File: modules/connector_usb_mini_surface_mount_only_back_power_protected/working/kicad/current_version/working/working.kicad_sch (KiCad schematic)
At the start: 2 parts, among them J3 scumnsmo

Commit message: a few module workings
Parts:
- removed D1: dssod123pmb2, oomlout_oomp_part_footprints:dssod123pmb2_electronic_diode_schottky_sod_123_package_marking_b2_mbr0520, symbol oomlout_oomp_part_symbols:dssod123pmb2_electronic_diode_schottky_sod_123_packag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
- removed J3: scumnsmo, oomlout_oomp_part_kicad_footprints:scumnsmo_electronic_socket_usb_mini_surface_mount_only, symbol oomlout_oomp_part_symbols:scumnsmo_electronic_socket_usb_mini_surface_mount_only
- added J1: scumnsmo, scumnsmo_electronic_socket_usb_mini_surface_mount_only, symbol oomlout_oomp_part_symbols:scumnsmo_electronic_socket_usb_mini_surface_mount_only
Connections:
- net +5V: now also J1.1 (VBUS)
- net GND: now also J1.5 (GND)
- net usb_id: now also J1.4 (ID)
- net usb_negative: now also J1.2 (D-)
- net usb_plus: now also J1.3 (D+)
- new net usb_shield: J1.6 (Shield)
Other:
- note added: "module connector usb_mini surface_mount_only"
- note removed: "module connector usb_mini surface_mount_only back_power_protected"
- note removed: "name"
- note removed: "usb_mini"
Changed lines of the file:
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@@
 (kicad_sch (version 20230121) (generator eeschema)
   (paper "A4")
-  (junction (at 146.05 114.3) (diameter 0) (color 0 0 0 0)
-  )
-  (wire (pts (xy 153.67 101.6) (xy 156.21 101.6))
+  (bus_entry (at 151.13 40.64) (size 2.54 2.54)
     (stroke (width 0) (type default))
   )
-  (wire (pts (xy 143.51 114.3) (xy 146.05 114.3))
+  (wire (pts (xy 175.26 69.85) (xy 172.72 69.85))
     (stroke (width 0) (type default))
   )
-  (wire (pts (xy 146.05 111.76) (xy 146.05 114.3))
+  (wire (pts (xy 165.1 85.09) (xy 165.1 87.63))
     (stroke (width 0) (type default))
   )
-  (wire (pts (xy 153.67 96.52) (xy 156.21 96.52))
+  (wire (pts (xy 162.56 85.09) (xy 162.56 87.63))
     (stroke (width 0) (type default))
   )
-  (wire (pts (xy 143.51 111.76) (xy 143.51 114.3))
+  (wire (pts (xy 172.72 74.93) (xy 175.26 74.93))
     (stroke (width 0) (type default))
   )
-  (wire (pts (xy 171.45 96.52) (xy 163.83 96.52))
+  (wire (pts (xy 172.72 80.01) (xy 175.26 80.01))
     (stroke (width 0) (type default))
   )
-  (wire (pts (xy 153.67 104.14) (xy 156.21 104.14))
+  (wire (pts (xy 175.26 67.31) (xy 175.26 69.85))
     (stroke (width 0) (type default))
   )
-  (wire (pts (xy 171.45 93.98) (xy 171.45 96.52))
+  (wire (pts (xy 172.72 77.47) (xy 175.26 77.47))
     (stroke (width 0) (type default))
   )
-  (wire (pts (xy 153.67 106.68) (xy 156.21 106.68))
-    (stroke (width 0) (type default))
-  )
-  (rectangle (start 143.51 64.77) (end 181.61 71.12)
-    (stroke (width 1) (type default))
-    (fill (type color) (color 0 0 0 0))
-  )
-  (rectangle (start 118.11 64.77) (end 181.61 129.54)
+  (rectangle (start 137.16 40.64) (end 200.66 105.41)
     (stroke (width 1) (type default))
     (fill (type none))
   )
-  (text "module\nconnector\nusb_mini\nsurface_mount_only\nback_power_protected\n"
-    (at 119.38 85.09 0)
+  (rectangle (start 199.39 97.79) (end 199.39 97.79)
+    (stroke (width 0) (type default))
+    (fill (type none))
+  )
+  (text "module\nconnector\nusb_mini\nsurface_mount_only\n\n" (at 138.43 60.96 0)
     (effects (font (size 2.5 2.5)) (justify left bottom))
   )
-  (text "usb_mini\n" (at 180.34 71.12 0)
-    (effects (font (size 4 4) (thickness 0.8) bold (color 255 255 255 1)) (justify right bottom))
-  )
-  (text "name" (at 146.05 71.12 90)
-    (effects (font (size 1.27 1.27) (thickness 0.254) bold (color 255 255 255 1)) (justify left bottom))
-  )
-  (label "usb_id" (at 156.21 106.68 0) (fields_autoplaced)
+  (label "usb_id" (at 175.26 80.01 0) (fields_autoplaced)
     (effects (font (size 1.27 1.27)) (justify left bottom))
   )
-  (label "usb_negative" (at 156.21 104.14 0) (fields_autoplaced)
+  (label "usb_plus" (at 175.26 74.93 0) (fields_autoplaced)
     (effects (font (size 1.27 1.27)) (justify left bottom))
   )
-  (label "usb_plus" (at 156.21 101.6 0) (fields_autoplaced)
+  (label "usb_negative" (at 175.26 77.47 0) (fields_autoplaced)
     (effects (font (size 1.27 1.27)) (justify left bottom))
   )
-  (symbol (lib_id "oomlout_oomp_part_symbols:scumnsmo_electronic_socket_usb_mini_surface_mount_only") (at 146.05 101.6 0) (unit 1)
+  (label "usb_shield" (at 162.56 87.63 270) (fields_autoplaced)
+    (effects (font (size 1.27 1.27)) (justify right bottom))
+  )
+  (symbol (lib_id "oomlout_oomp_part_symbols:scumnsmo_electronic_socket_usb_mini_surface_mount_only") (at 165.1 74.93 0) (unit 1)
     (in_bom yes) (on_board yes) (dnp no) (fields_autoplaced)
-    (property "Reference" "J3" (at 146.05 88.9 0)
+    (property "Reference" "J1" (at 165.1 62.23 0)
       (effects (font (size 1.27 1.27)))
     )
-    (property "Value" "scumnsmo" (at 146.05 91.44 0)
+    (property "Value" "scumnsmo" (at 165.1 64.77 0)
       (effects (font (size 1.27 1.27)))
     )
-    (property "Footprint" "oomlout_oomp_part_kicad_footprints:scumnsmo_electronic_socket_usb_mini_surface_mount_only" (at 149.86 102.87 0)
+    (property "Footprint" "scumnsmo_electronic_socket_usb_mini_surface_mount_only" (at 168.91 76.2 0)
       (effects (font (size 1.27 1.27)) hide)
     )
-    (property "Datasheet" "https://github.com/oomlout/oomlout_oomp_v3/parts/electronic_socket_usb_mini_surface_mount_only/datasheet.pdf" (at 149.86 102.87 0)
+    (property "Datasheet" "https://github.com/oomlout/oomlout_oomp_v3/parts/electronic_socket_usb_mini_surface_mount_only/datasheet.pdf" (at 168.91 76.2 0)
       (effects (font (size 1.27 1.27)) hide)
     )
@@
     (instances
       (project "working"
-        (path "/5407c114-4107-4d84-8382-1717fb9d687c"
-          (reference "J3") (unit 1)
-        )
-      )
-      (project "working"
         (path "/d7ac9d55-1973-40f4-b2a5-38a433b49fa0"
           (reference "J1") (unit 1)
@@
     )
   )
-  (symbol (lib_id "oomlout_oomp_part_symbols:dssod123pmb2_electronic_diode_schottky_sod_123_package_marking_b2_mbr0520") (at 160.02 96.52 180) (unit 1)
+  (symbol (lib_id "power:+5V") (at 175.26 67.31 0) (unit 1)
     (in_bom yes) (on_board yes) (dnp no) (fields_autoplaced)
-    (property "Reference" "D1" (at 160.3375 90.17 0)
+    (property "Reference" "#PWR04" (at 175.26 71.12 0)
+      (effects (font (size 1.27 1.27)) hide)
+    )
+    (property "Value" "+5V" (at 175.26 62.23 0)
       (effects (font (size 1.27 1.27)))
     )
-    (property "Value" "dssod123pmb2" (at 160.3375 92.71 0)
-      (effects (font (size 1.27 1.27)))
-    )
-    (property "Footprint" "oomlout_oomp_part_footprints:dssod123pmb2_electronic_diode_schottky_sod_123_package_marking_b2_mbr0520" (at 160.02 96.52 0)
+    (property "Footprint" "" (at 175.26 67.31 0)
       (effects (font (size 1.27 1.27)) hide)
     )
-    (property "Datasheet" "https://github.com/oomlout/oomlout_oomp_v3/parts/electronic_diode_schottky_sod_123_package_marking_b2_mbr0520/datasheet.pdf" (at 160.02 96.52 0)
-      (effects (font (size 1.27 1.27)) hide)
-    )
-    (pin "1")
-    (pin "2")
-    (instances
-      (project "working"
-        (path "/d7ac9d55-1973-40f4-b2a5-38a433b49fa0"
-          (reference "D1") (unit 1)
-        )
-      )
-    )
-  )
-  (symbol (lib_id "power:+5V") (at 171.45 93.98 0) (unit 1)
-    (in_bom yes) (on_board yes) (dnp no) (fields_autoplaced)
-    (property "Reference" "#PWR013" (at 171.45 97.79 0)
-      (effects (font (size 1.27 1.27)) hide)
-    )
-    (property "Value" "+5V" (at 171.45 88.9 0)
-      (effects (font (size 1.27 1.27)))
-    )
-    (property "Footprint" "" (at 171.45 93.98 0)
-      (effects (font (size 1.27 1.27)) hide)
-    )
-    (property "Datasheet" "" (at 171.45 93.98 0)
+    (property "Datasheet" "" (at 175.26 67.31 0)
       (effects (font (size 1.27 1.27)) hide)
     )
@@
     (instances
       (project "working"
-        (path "/5407c114-4107-4d84-8382-1717fb9d687c"
-          (reference "#PWR013") (unit 1)
-        )
-      )
-      (project "working"
         (path "/d7ac9d55-1973-40f4-b2a5-38a433b49fa0"
-          (reference "#PWR02") (unit 1)
+          (reference "#PWR04") (unit 1)
         )
       )
     )
   )
-  (symbol (lib_id "power:GND") (at 146.05 114.3 0) (unit 1)
+  (symbol (lib_id "power:GND") (at 165.1 87.63 0) (unit 1)
     (in_bom yes) (on_board yes) (dnp no) (fields_autoplaced)
-    (property "Reference" "#PWR012" (at 146.05 120.65 0)
+    (property "Reference" "#PWR03" (at 165.1 93.98 0)
       (effects (font (size 1.27 1.27)) hide)
     )
-    (property "Value" "GND" (at 146.05 119.38 0)
+    (property "Value" "GND" (at 165.1 92.71 0)
       (effects (font (size 1.27 1.27)))
     )
-    (property "Footprint" "" (at 146.05 114.3 0)
+    (property "Footprint" "" (at 165.1 87.63 0)
       (effects (font (size 1.27 1.27)) hide)
     )
-    (property "Datasheet" "" (at 146.05 114.3 0)
+    (property "Datasheet" "" (at 165.1 87.63 0)
       (effects (font (size 1.27 1.27)) hide)
     )
@@
     (instances
       (project "working"
-        (path "/5407c114-4107-4d84-8382-1717fb9d687c"
-          (reference "#PWR012") (unit 1)
+        (path "/d7ac9d55-1973-40f4-b2a5-38a433b49fa0"
+          (reference "#PWR03") (unit 1)
         )
       )
-      (project "working"
-        (path "/d7ac9d55-1973-40f4-b2a5-38a433b49fa0"
-          (reference "#PWR01") (unit 1)
-        )
-      )

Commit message: works.
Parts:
- added D1: dssod123pmb2mbr0520, oomlout_oomp_part_footprints:dssod123pmb2mbr0520_electronic_diode_schottky_sod_123_package_marking_b2_mbr0520, symbol oomlout_oomp_part_symbols:dssod123pmb2mbr0520_electronic_diode_schottky_sod_123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
- J1: footprint scumnsmo_electronic_socket_usb_mini_surface_mount_only -> oomlout_oomp_part_footprints:scumnsmo_electronic_socket_usb_mini_surface_mount_only
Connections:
- net usb_shield is gone; now on net GND: J1.6 (Shield)
- net +5V: now also D1.1 (K); no longer J1.1 (VBUS)
- net usb_plus renamed usb_positive
- new net: D1.2 (A), J1.1 (VBUS)
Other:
- note added: "module connector usb_mini surface_mount_only back_power_protected"
- note added: "name"
- note added: "usb_mini_bp"
- note removed: "module connector usb_mini surface_mount_only"
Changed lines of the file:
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@@
 (kicad_sch (version 20230121) (generator eeschema)
   (paper "A4")
-  (bus_entry (at 151.13 40.64) (size 2.54 2.54)
+  (junction (at 129.54 105.41) (diameter 0) (color 0 0 0 0)
+  )
+  (wire (pts (xy 129.54 102.87) (xy 129.54 105.41))
     (stroke (width 0) (type default))
   )
-  (wire (pts (xy 175.26 69.85) (xy 172.72 69.85))
+  (wire (pts (xy 137.16 87.63) (xy 139.7 87.63))
     (stroke (width 0) (type default))
   )
-  (wire (pts (xy 165.1 85.09) (xy 165.1 87.63))
+  (wire (pts (xy 137.16 97.79) (xy 139.7 97.79))
     (stroke (width 0) (type default))
   )
-  (wire (pts (xy 162.56 85.09) (xy 162.56 87.63))
+  (wire (pts (xy 137.16 95.25) (xy 139.7 95.25))
     (stroke (width 0) (type default))
   )
-  (wire (pts (xy 172.72 74.93) (xy 175.26 74.93))
+  (wire (pts (xy 154.94 85.09) (xy 154.94 87.63))
     (stroke (width 0) (type default))
   )
-  (wire (pts (xy 172.72 80.01) (xy 175.26 80.01))
+  (wire (pts (xy 154.94 87.63) (xy 147.32 87.63))
     (stroke (width 0) (type default))
   )
-  (wire (pts (xy 175.26 67.31) (xy 175.26 69.85))
+  (wire (pts (xy 127 105.41) (xy 129.54 105.41))
     (stroke (width 0) (type default))
   )
-  (wire (pts (xy 172.72 77.47) (xy 175.26 77.47))
+  (wire (pts (xy 127 102.87) (xy 127 105.41))
     (stroke (width 0) (type default))
   )
-  (rectangle (start 137.16 40.64) (end 200.66 105.41)
+  (wire (pts (xy 137.16 92.71) (xy 139.7 92.71))
+    (stroke (width 0) (type default))
+  )
+  (rectangle (start 127 55.88) (end 165.1 62.23)
+    (stroke (width 1) (type default))
+    (fill (type color) (color 0 0 0 0))
+  )
+  (rectangle (start 101.6 55.88) (end 165.1 120.65)
     (stroke (width 1) (type default))
     (fill (type none))
   )
-  (rectangle (start 199.39 97.79) (end 199.39 97.79)
-    (stroke (width 0) (type default))
-    (fill (type none))
+  (text "usb_mini_bp\n\n" (at 165.1 66.04 0)
+    (effects (font (size 3 3) (thickness 0.8) bold (color 255 255 255 1)) (justify right bottom))
   )
-  (text "module\nconnector\nusb_mini\nsurface_mount_only\n\n" (at 138.43 60.96 0)
+  (text "name" (at 129.54 62.23 90)
+    (effects (font (size 1.27 1.27) (thickness 0.254) bold (color 255 255 255 1)) (justify left bottom))
+  )
+  (text "module\nconnector\nusb_mini\nsurface_mount_only\nback_power_protected\n"
+    (at 102.87 76.2 0)
     (effects (font (size 2.5 2.5)) (justify left bottom))
   )
-  (label "usb_id" (at 175.26 80.01 0) (fields_autoplaced)
+  (label "usb_positive" (at 139.7 92.71 0) (fields_autoplaced)
     (effects (font (size 1.27 1.27)) (justify left bottom))
   )
-  (label "usb_plus" (at 175.26 74.93 0) (fields_autoplaced)
+  (label "usb_negative" (at 139.7 95.25 0) (fields_autoplaced)
     (effects (font (size 1.27 1.27)) (justify left bottom))
   )
-  (label "usb_negative" (at 175.26 77.47 0) (fields_autoplaced)
+  (label "usb_id" (at 139.7 97.79 0) (fields_autoplaced)
     (effects (font (size 1.27 1.27)) (justify left bottom))
   )
-  (label "usb_shield" (at 162.56 87.63 270) (fields_autoplaced)
-    (effects (font (size 1.27 1.27)) (justify right bottom))
-  )
-  (symbol (lib_id "oomlout_oomp_part_symbols:scumnsmo_electronic_socket_usb_mini_surface_mount_only") (at 165.1 74.93 0) (unit 1)
+  (symbol (lib_id "oomlout_oomp_part_symbols:dssod123pmb2mbr0520_electronic_diode_schottky_sod_123_package_marking_b2_mbr0520") (at 143.51 87.63 180) (unit 1)
     (in_bom yes) (on_board yes) (dnp no) (fields_autoplaced)
-    (property "Reference" "J1" (at 165.1 62.23 0)
+    (property "Reference" "D1" (at 143.8275 82.55 0)
       (effects (font (size 1.27 1.27)))
     )
-    (property "Value" "scumnsmo" (at 165.1 64.77 0)
+    (property "Value" "dssod123pmb2mbr0520" (at 143.8275 85.09 0)
+      (effects (font (size 0.75 0.75)))
+    )
+    (property "Footprint" "oomlout_oomp_part_footprints:dssod123pmb2mbr0520_electronic_diode_schottky_sod_123_package_marking_b2_mbr0520" (at 143.51 87.63 0)
+      (effects (font (size 1.27 1.27)) hide)
+    )
+    (property "Datasheet" "https://github.com/oomlout/oomlout_oomp_v3/parts/electronic_diode_schottky_sod_123_package_marking_b2_mbr0520/datasheet.pdf" (at 143.51 87.63 0)
+      (effects (font (size 1.27 1.27)) hide)
+    )
+    (pin "1")
+    (pin "2")
+    (instances
+      (project "working"
+        (path "/d7ac9d55-1973-40f4-b2a5-38a433b49fa0"
+          (reference "D1") (unit 1)
+        )
+      )
+    )
+  )
+  (symbol (lib_id "power:+5V") (at 154.94 85.09 0) (unit 1)
+    (in_bom yes) (on_board yes) (dnp no) (fields_autoplaced)
+    (property "Reference" "#PWR013" (at 154.94 88.9 0)
+      (effects (font (size 1.27 1.27)) hide)
+    )
+    (property "Value" "+5V" (at 154.94 80.01 0)
       (effects (font (size 1.27 1.27)))
     )
-    (property "Footprint" "scumnsmo_electronic_socket_usb_mini_surface_mount_only" (at 168.91 76.2 0)
+    (property "Footprint" "" (at 154.94 85.09 0)
       (effects (font (size 1.27 1.27)) hide)
     )
-    (property "Datasheet" "https://github.com/oomlout/oomlout_oomp_v3/parts/electronic_socket_usb_mini_surface_mount_only/datasheet.pdf" (at 168.91 76.2 0)
+    (property "Datasheet" "" (at 154.94 85.09 0)
+      (effects (font (size 1.27 1.27)) hide)
+    )
+    (pin "1")
+    (instances
+      (project "working"
+        (path "/5407c114-4107-4d84-8382-1717fb9d687c"
+          (reference "#PWR013") (unit 1)
+        )
+      )
+      (project "working"
+        (path "/d7ac9d55-1973-40f4-b2a5-38a433b49fa0"
+          (reference "#PWR02") (unit 1)
+        )
+      )
+    )
+  )
+  (symbol (lib_id "oomlout_oomp_part_symbols:scumnsmo_electronic_socket_usb_mini_surface_mount_only") (at 129.54 92.71 0) (unit 1)
+    (in_bom yes) (on_board yes) (dnp no) (fields_autoplaced)
+    (property "Reference" "J1" (at 129.54 80.01 0)
+      (effects (font (size 1.27 1.27)))
+    )
+    (property "Value" "scumnsmo" (at 129.54 82.55 0)
+      (effects (font (size 1.27 1.27)))
+    )
+    (property "Footprint" "oomlout_oomp_part_footprints:scumnsmo_electronic_socket_usb_mini_surface_mount_only" (at 133.35 93.98 0)
+      (effects (font (size 1.27 1.27)) hide)
+    )
+    (property "Datasheet" "https://github.com/oomlout/oomlout_oomp_v3/parts/electronic_socket_usb_mini_surface_mount_only/datasheet.pdf" (at 133.35 93.98 0)
       (effects (font (size 1.27 1.27)) hide)
     )
@@
     )
   )
-  (symbol (lib_id "power:+5V") (at 175.26 67.31 0) (unit 1)
+  (symbol (lib_id "power:GND") (at 129.54 105.41 0) (unit 1)
     (in_bom yes) (on_board yes) (dnp no) (fields_autoplaced)
-    (property "Reference" "#PWR04" (at 175.26 71.12 0)
+    (property "Reference" "#PWR012" (at 129.54 111.76 0)
       (effects (font (size 1.27 1.27)) hide)
     )
-    (property "Value" "+5V" (at 175.26 62.23 0)
+    (property "Value" "GND" (at 129.54 110.49 0)
       (effects (font (size 1.27 1.27)))
     )
-    (property "Footprint" "" (at 175.26 67.31 0)
+    (property "Footprint" "" (at 129.54 105.41 0)
       (effects (font (size 1.27 1.27)) hide)
     )
-    (property "Datasheet" "" (at 175.26 67.31 0)
+    (property "Datasheet" "" (at 129.54 105.41 0)
       (effects (font (size 1.27 1.27)) hide)
     )
@@
     (instances
       (project "working"
-        (path "/d7ac9d55-1973-40f4-b2a5-38a433b49fa0"
-          (reference "#PWR04") (unit 1)
+        (path "/5407c114-4107-4d84-8382-1717fb9d687c"
+          (reference "#PWR012") (unit 1)
         )
       )
-    )
-  )
-  (symbol (lib_id "power:GND") (at 165.1 87.63 0) (unit 1)
-    (in_bom yes) (on_board yes) (dnp no) (fields_autoplaced)
-    (property "Reference" "#PWR03" (at 165.1 93.98 0)
-      (effects (font (size 1.27 1.27)) hide)
-    )
-    (property "Value" "GND" (at 165.1 92.71 0)
-      (effects (font (size 1.27 1.27)))
-    )
-    (property "Footprint" "" (at 165.1 87.63 0)
-      (effects (font (size 1.27 1.27)) hide)
-    )
-    (property "Datasheet" "" (at 165.1 87.63 0)
-      (effects (font (size 1.27 1.27)) hide)
-    )
-    (pin "1")
-    (instances
       (project "working"
         (path "/d7ac9d55-1973-40f4-b2a5-38a433b49fa0"
-          (reference "#PWR03") (unit 1)
+          (reference "#PWR01") (unit 1)
         )
       )

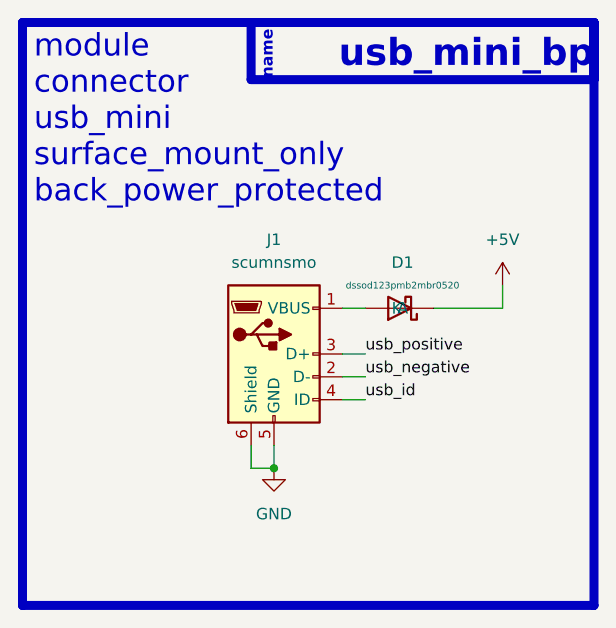
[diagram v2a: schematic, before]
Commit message: fixed formatting to be more consistent
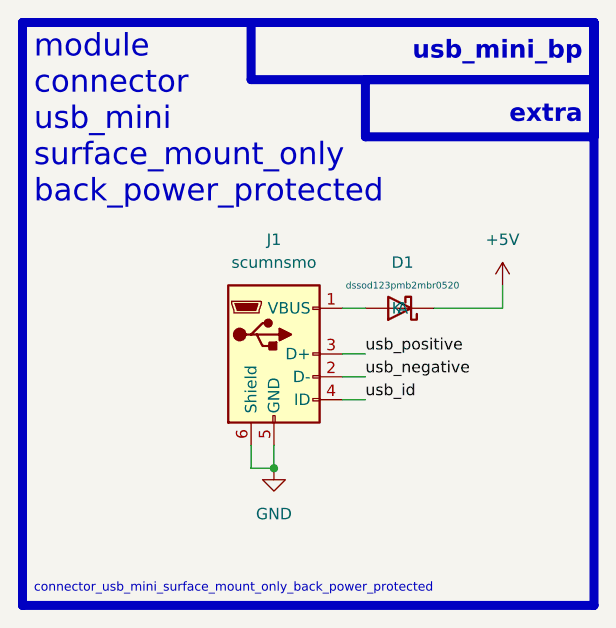
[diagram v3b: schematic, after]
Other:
- note added: "connector_usb_mini_surface_mount_only_back_power_protected"
- note added: "extra"
- note removed: "name"
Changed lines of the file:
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@@
   (rectangle (start 127 55.88) (end 165.1 62.23)
     (stroke (width 1) (type default))
-    (fill (type color) (color 0 0 0 0))
+    (fill (type none))
   )
   (rectangle (start 101.6 55.88) (end 165.1 120.65)
@@
     (fill (type none))
   )
-  (text "usb_mini_bp\n\n" (at 165.1 66.04 0)
-    (effects (font (size 3 3) (thickness 0.8) bold (color 255 255 255 1)) (justify right bottom))
+  (rectangle (start 139.7 62.23) (end 165.1 68.58)
+    (stroke (width 1) (type default))
+    (fill (type none))
   )
-  (text "name" (at 129.54 62.23 90)
-    (effects (font (size 1.27 1.27) (thickness 0.254) bold (color 255 255 255 1)) (justify left bottom))
+  (text "usb_mini_bp\n\n" (at 163.83 63.5 0)
+    (effects (font (size 2 2) (thickness 0.8) bold) (justify right bottom))
+  )
+  (text "connector_usb_mini_surface_mount_only_back_power_protected"
+    (at 102.87 119.38 0)
+    (effects (font (size 1 1)) (justify left bottom))
   )
   (text "module\nconnector\nusb_mini\nsurface_mount_only\nback_power_protected\n"
@@
     (effects (font (size 2.5 2.5)) (justify left bottom))
   )
+  (text "extra" (at 163.83 67.31 0)
+    (effects (font (size 2 2) (thickness 0.8) bold) (justify right bottom))
+  )
   (label "usb_positive" (at 139.7 92.71 0) (fields_autoplaced)
